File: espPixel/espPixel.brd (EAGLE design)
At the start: 39.3 x 80 mm, 85 parts, among them IC1 74LVC1T45GW,125, IC2 74LVC1T45GW,125, IC3 MP2315GJ-Z, IC4 CP2104, J1 TBLH10-350-04BK, J2 TBLH10-350-03BK, J3 TBLH10-350-02BK, Q1 SIR414DP-T1-GE3, Q2 SIR414DP-T1-GE3, Q5 mmbt2222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

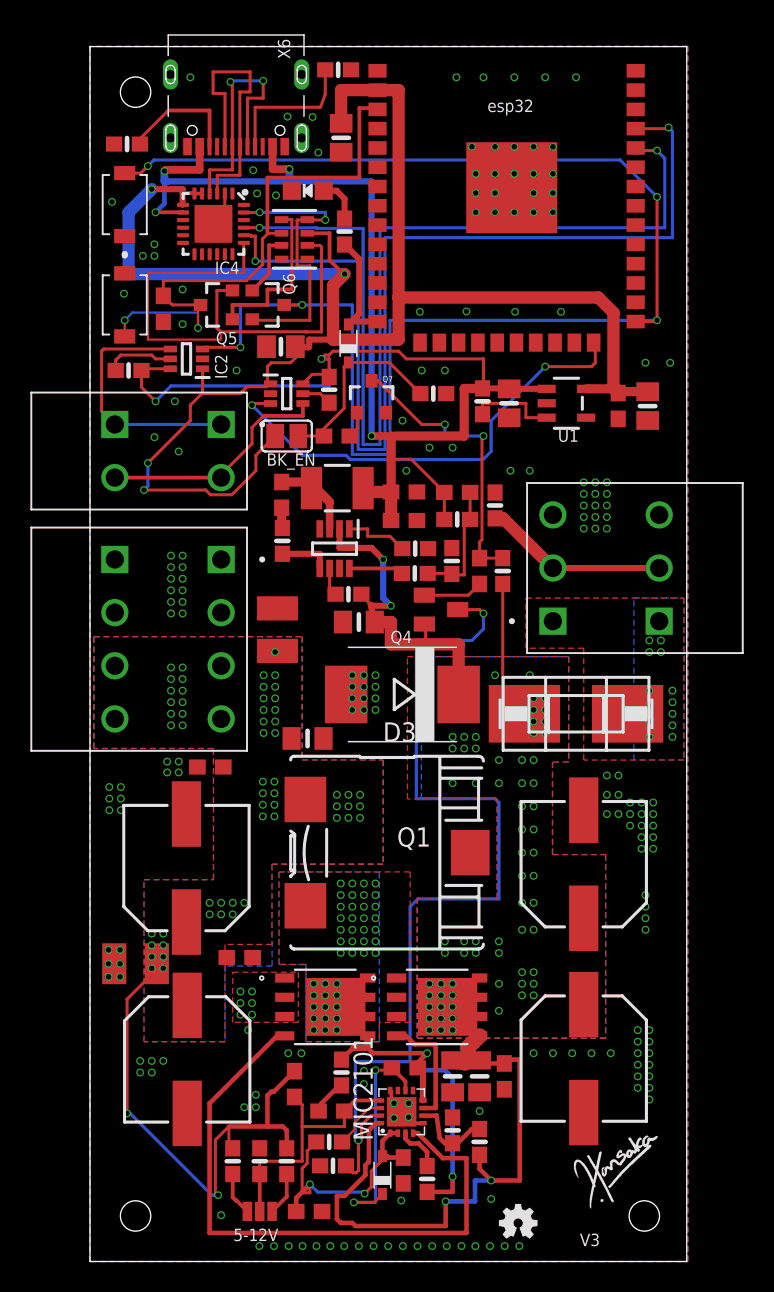
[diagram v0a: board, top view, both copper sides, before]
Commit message: v3 more compact size
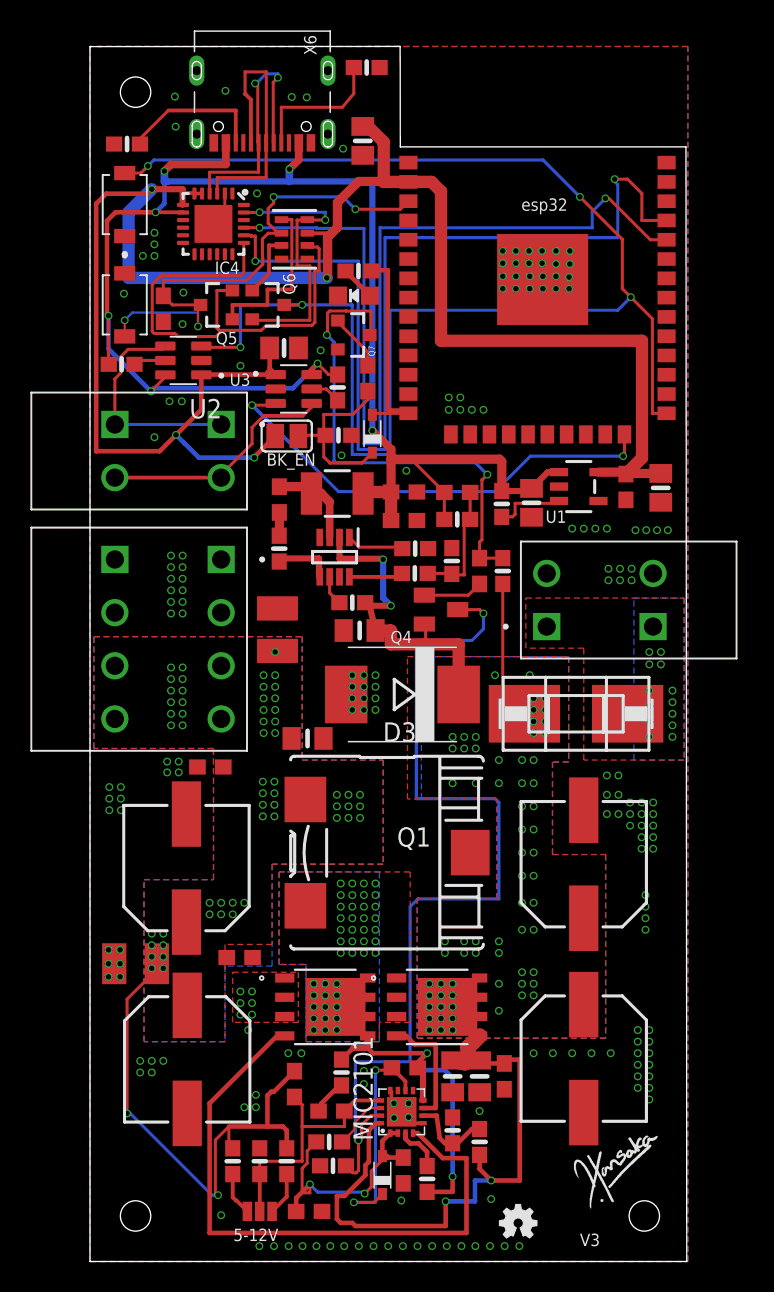
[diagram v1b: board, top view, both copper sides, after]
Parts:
- removed IC1, IC2: 74LVC1T45GW,125, 74LVC1T45GW_125:SOP65P210X110-6N
- removed R18, R26: 50K, microbuilder:0603-NO
- added R27: 50K, microbuilder:0603-NO
- added U2, U3: 74LVC1T45W6-7, 74LVC1T45W6-7:SOT95P285X140-6N
- J2: value TBLH10-350-03BK -> TBLH10-350-02BK; device TBLH10-350-03BK:CUI_TBLH10-350-03BK -> TBLH10-350-02BK:CUI_TBLH10-350-02BK
- R16: value 10 -> 50K
- moved R16 26.3 mm to (2.08, 59.1), turned to 180 degrees
- moved D13 7.55 mm to (17.4, 63.6)
- moved R17 6.87 mm to (27.1, 49.9)
- moved R20 6.82 mm to (16.4, 54.4)
- moved C16 6.72 mm to (29.1, 50.0)
- moved X8 6.38 mm to (29.5, 67.4)
- moved D2 6.15 mm to (18.6, 54.5)
- moved U1 5.55 mm to (32.2, 51.0)
- moved C18 5.45 mm to (37.6, 50.9)
- moved C17 5.36 mm to (35.3, 51.0)
- moved R6 4.32 mm to (18.3, 58.2), turned to 270 degrees
- moved Q7 4.29 mm to (17.3, 61.0), turned to 270 degrees
- moved R43 2.75 mm to (17.7, 65.2), turned to 180 degrees
- moved R22 1.89 mm to (18.2, 78.6)
- moved X6 1.75 mm to (11.3, 77.2)
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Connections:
- net N$20 renamed PWIN
- removed net N$16: IC2.5, R26.2
- removed net N$19: J2.2_A, J2.2_B, R16.1
- removed net N$22: IC1.5, R18.2
- new net N$10: R27.1, U3.5
- new net N$28: R16.1, U2.5
- net 3.3V: now also U2.1, U3.1; no longer IC1.1, IC2.1
- net GND: now also J2.2_A, J2.2_B, U2.2, U3.2; no longer IC1.2, IC2.2, J2.3_A, J2.3_B, R16.2
- net GPIO0: now also U2.3; no longer IC2.3
- net GPIO0_5V: now also U2.4; no longer IC2.4
- net NEODATA_3V: now also U3.3; no longer IC1.3
- net NEODATA_5V: now also U3.4; no longer IC1.4
- net VBUS: now also R16.2, R27.2, U2.6, U3.6; no longer IC1.6, IC2.6, R18.1, R26.1
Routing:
- net N$26: track 19.0 -> 32.6 mm
- net N$19: track 12.2 -> 0.00 mm
- net 3.3V: track 120.4 -> 128.2 mm
- net GPIO12: track 8.07 -> 14.1 mm
- net NEODATA_3V: track 30.6 -> 35.7 mm
- net N$16: track 4.52 -> 0.00 mm
- net RXD0: track 63.1 -> 58.8 mm
- net TXD0: track 65.9 -> 62.2 mm
- net RESET: track 38.2 -> 34.7 mm, vias 2 -> 4
- net GND: track 10.3 -> 7.21 mm, vias 198 -> 192
- net RTS: track 35.0 -> 32.6 mm
- net N$28: track 0.00 -> 2.13 mm
- net N$10: track 0.00 -> 2.02 mm
- net N$23: track 1.74 -> 3.76 mm
- net N$22: track 1.98 -> 0.00 mm
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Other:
- outline, holes or cut-outs redrawn
- board text removed: "PW-EN"
